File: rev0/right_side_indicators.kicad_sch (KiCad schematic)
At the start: 30 parts, among them IC1 ECP5-BGA256, U14 74AUP2G126, U2 74AUP2G126

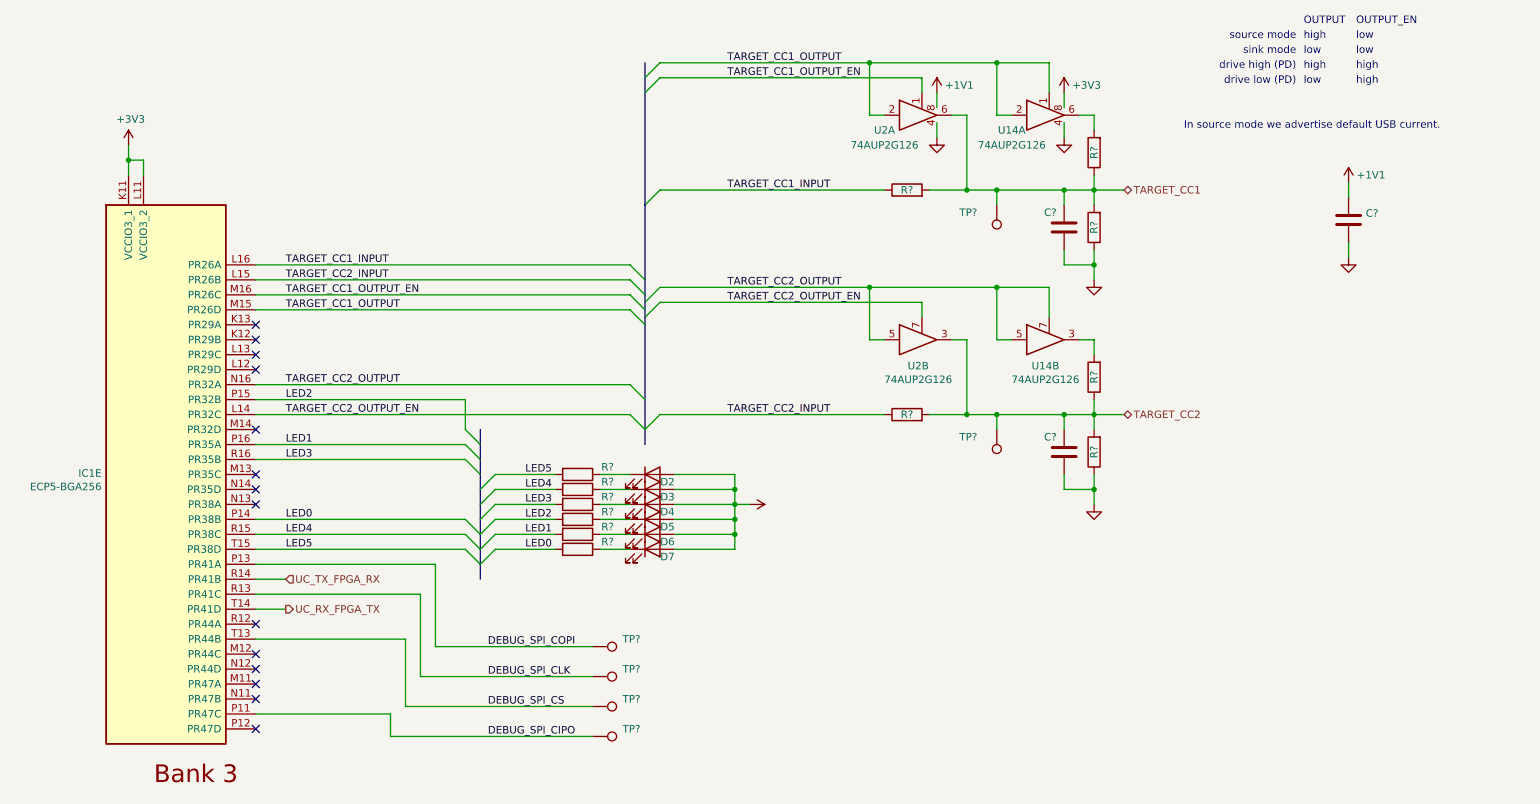
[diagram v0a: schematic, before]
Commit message: hardware: update 3D model paths for KiCad 6
see: https://gitlab.com/kicad/code/kicad/-/issues/10674
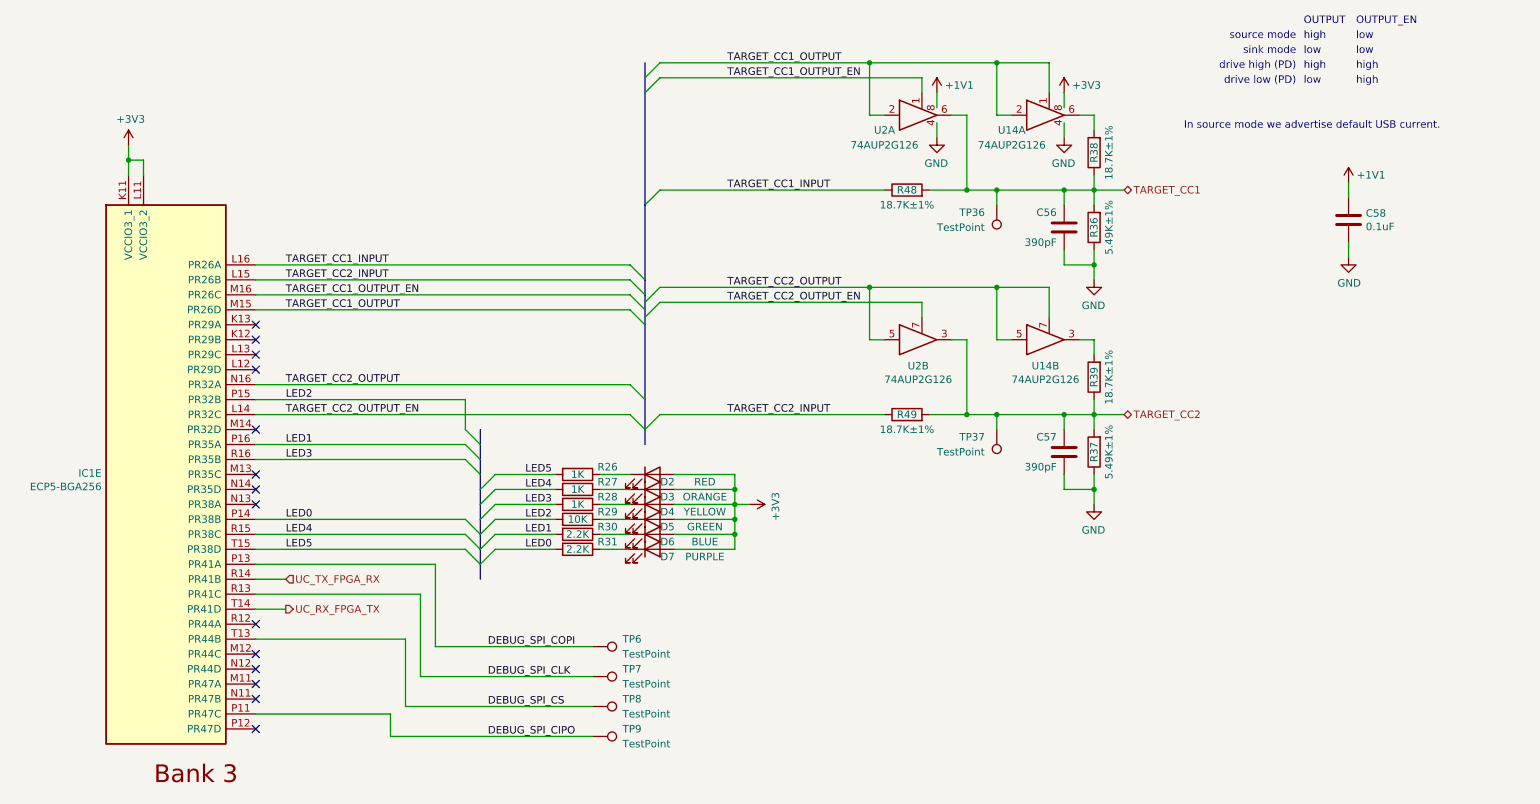
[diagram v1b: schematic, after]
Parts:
- C56, C57: renamed from C?; value (none) -> 390pF; footprint (none) -> Capacitor_SMD:C_0402_1005Metric
- C58: renamed from C?; value (none) -> 0.1uF; footprint (none) -> Capacitor_SMD:C_0402_1005Metric
- D2: value (none) -> RED; footprint (none) -> LED_SMD:LED_0603_1608Metric_Pad1.05x0.95mm_HandSolder
- D3: value (none) -> ORANGE; footprint (none) -> LED_SMD:LED_0603_1608Metric_Pad1.05x0.95mm_HandSolder
- D4: value (none) -> YELLOW; footprint (none) -> LED_SMD:LED_0603_1608Metric_Pad1.05x0.95mm_HandSolder
- D5: value (none) -> GREEN; footprint (none) -> LED_SMD:LED_0603_1608Metric_Pad1.05x0.95mm_HandSolder
- D6: value (none) -> BLUE; footprint (none) -> LED_SMD:LED_0603_1608Metric_Pad1.05x0.95mm_HandSolder
- D7: value (none) -> PURPLE; footprint (none) -> LED_SMD:LED_0603_1608Metric_Pad1.05x0.95mm_HandSolder
- R26, R27, R28: renamed from R?; value (none) -> 1K; footprint (none) -> Resistor_SMD:R_0402_1005Metric
- R29: renamed from R?; value (none) -> 10K; footprint (none) -> Resistor_SMD:R_0402_1005Metric
- R30, R31: renamed from R?; value (none) -> 2.2K; footprint (none) -> Resistor_SMD:R_0402_1005Metric
- R36, R37: renamed from R?; value (none) -> 5.49K±1%; footprint (none) -> Resistor_SMD:R_0402_1005Metric
- R38, R39, R48, R49: renamed from R?; value (none) -> 18.7K±1%; footprint (none) -> Resistor_SMD:R_0402_1005Metric
- TP36, TP37, TP6, TP7, TP8, TP9: renamed from TP?; value (none) -> TestPoint; footprint (none) -> TestPoint:TestPoint_Pad_D1.0mm

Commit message: hardware: update silkscreen, dates, title blocks
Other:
- company: Copyright 2019-2021 Great Scott Gadgets -> Copyright 2019-2023 Great Scott Gadgets
- title: LUNA: Right Side I/O -> LUNA USB Multitool
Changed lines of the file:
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@@
   (paper "A4")
   (title_block
-    (title "LUNA: Right Side I/O")
-    (date "2021-03-10")
-    (rev "r0")
-    (company "Copyright 2019-2021 Great Scott Gadgets")
-    (comment 1 "Katherine J. Temkin")
-    (comment 3 "Licensed under the CERN-OHL-P v2")
+    (title "LUNA USB Multitool")
+    (date "2023-01-11")
+    (rev "r0.5")
+    (company "Copyright 2019-2023 Great Scott Gadgets")
+    (comment 1 "Licensed under the CERN-OHL-P v2")
   )
   (junction (at 201.93 88.9) (diameter 0) (color 0 0 0 0)

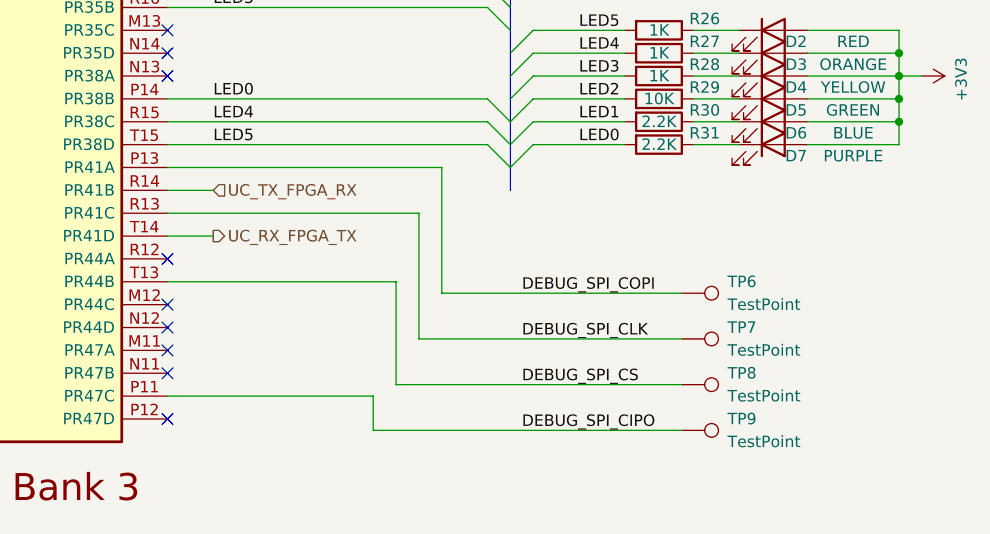
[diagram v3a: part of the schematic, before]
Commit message: hardware: remove debug SPI interface
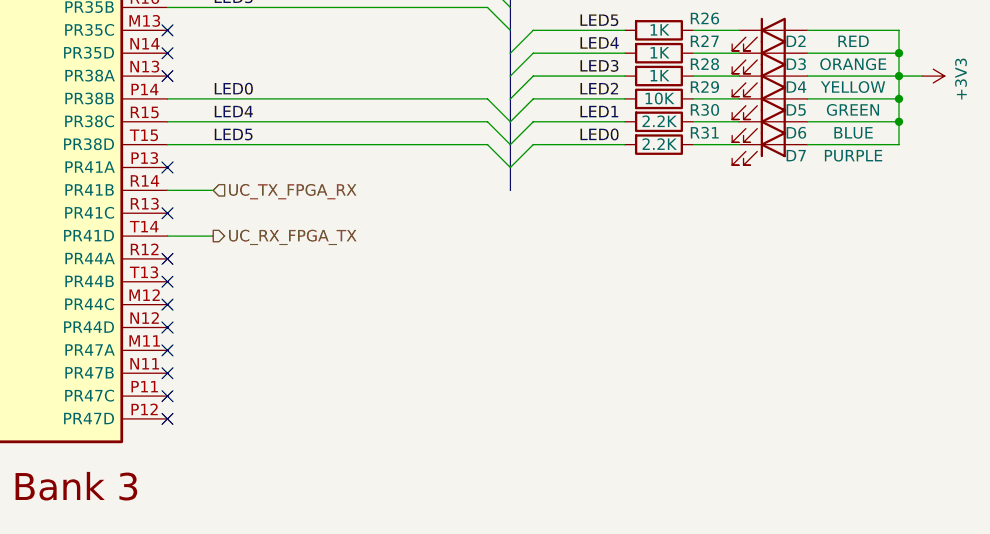
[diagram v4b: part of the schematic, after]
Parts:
- removed TP6, TP7, TP8, TP9: TestPoint, TestPoint:TestPoint_Pad_D1.0mm, symbol Connector:TestPoint
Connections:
- net DEBUG_SPI_CIPO: no longer names the net of IC1.P11 (PR47C)
- net DEBUG_SPI_CLK: no longer names the net of IC1.R13 (PR41C)
- net DEBUG_SPI_COPI: no longer names the net of IC1.P13 (PR41A)
- net DEBUG_SPI_CS: no longer names the net of IC1.T13 (PR44B)
- no-connect marks 14 -> 18
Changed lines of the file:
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@@
   )
   (no_connect (at 76.2 101.6))
+  (no_connect (at 76.2 119.38))
+  (no_connect (at 76.2 127))
   (no_connect (at 76.2 137.16))
   (no_connect (at 76.2 81.28))
   (no_connect (at 76.2 132.08))
+  (no_connect (at 76.2 139.7))
   (no_connect (at 76.2 76.2))
   (no_connect (at 76.2 134.62))
   (no_connect (at 76.2 104.14))
   (no_connect (at 76.2 129.54))
+  (no_connect (at 76.2 114.3))
   (no_connect (at 76.2 73.66))
   (no_connect (at 76.2 78.74))
@@
     (stroke (width 0) (type default) (color 0 0 0 0))
   )
-  (wire (pts (xy 99.06 143.51) (xy 99.06 139.7))
-    (stroke (width 0) (type default) (color 0 0 0 0))
-  )
   (wire (pts (xy 196.85 88.9) (xy 190.5 88.9))
     (stroke (width 0) (type default) (color 0 0 0 0))
@@
     (stroke (width 0) (type default) (color 0 0 0 0))
   )
-  (wire (pts (xy 76.2 127) (xy 101.6 127))
-    (stroke (width 0) (type default) (color 0 0 0 0))
-  )
   (wire (pts (xy 157.48 99.06) (xy 157.48 101.6))
     (stroke (width 0) (type default) (color 0 0 0 0))
@@
     (stroke (width 0) (type default) (color 0 0 0 0))
   )
-  (wire (pts (xy 104.14 133.35) (xy 133.35 133.35))
-    (stroke (width 0) (type default) (color 0 0 0 0))
-  )
   (bus (pts (xy 114.3 99.06) (xy 114.3 101.6))
     (stroke (width 0) (type default) (color 0 0 0 0))
@@
     (stroke (width 0) (type default) (color 0 0 0 0))
   )
-  (wire (pts (xy 106.68 128.27) (xy 106.68 114.3))
-    (stroke (width 0) (type default) (color 0 0 0 0))
-  )
   (wire (pts (xy 218.44 63.5) (xy 218.44 66.04))
     (stroke (width 0) (type default) (color 0 0 0 0))
@@
     (stroke (width 0) (type default) (color 0 0 0 0))
   )
-  (wire (pts (xy 104.14 119.38) (xy 104.14 133.35))
-    (stroke (width 0) (type default) (color 0 0 0 0))
-  )
-  (wire (pts (xy 101.6 138.43) (xy 101.6 127))
-    (stroke (width 0) (type default) (color 0 0 0 0))
-  )
   (bus (pts (xy 114.3 104.14) (xy 114.3 106.68))
     (stroke (width 0) (type default) (color 0 0 0 0))
@@
     (stroke (width 0) (type default) (color 0 0 0 0))
   )
-  (wire (pts (xy 76.2 114.3) (xy 106.68 114.3))
-    (stroke (width 0) (type default) (color 0 0 0 0))
-  )
   (wire (pts (xy 223.52 88.9) (xy 218.44 88.9))
     (stroke (width 0) (type default) (color 0 0 0 0))
@@
     (stroke (width 0) (type default) (color 0 0 0 0))
   )
-  (wire (pts (xy 76.2 139.7) (xy 99.06 139.7))
-    (stroke (width 0) (type default) (color 0 0 0 0))
-  )
   (wire (pts (xy 116.84 109.22) (xy 127 109.22))
     (stroke (width 0) (type default) (color 0 0 0 0))
@@
     (stroke (width 0) (type default) (color 0 0 0 0))
   )
-  (wire (pts (xy 133.35 143.51) (xy 99.06 143.51))
-    (stroke (width 0) (type default) (color 0 0 0 0))
-  )
   (bus (pts (xy 142.24 72.39) (xy 142.24 73.66))
     (stroke (width 0) (type default) (color 0 0 0 0))
@@
     (stroke (width 0) (type default) (color 0 0 0 0))
   )
-  (wire (pts (xy 106.68 128.27) (xy 133.35 128.27))
-    (stroke (width 0) (type default) (color 0 0 0 0))
-  )
   (wire (pts (xy 190.5 50.8) (xy 196.85 50.8))
     (stroke (width 0) (type default) (color 0 0 0 0))
@@
     (stroke (width 0) (type default) (color 0 0 0 0))
   )
-  (wire (pts (xy 101.6 138.43) (xy 133.35 138.43))
-    (stroke (width 0) (type default) (color 0 0 0 0))
-  )
   (wire (pts (xy 218.44 63.5) (xy 213.36 63.5))
     (stroke (width 0) (type default) (color 0 0 0 0))
@@
   )
   (wire (pts (xy 157.48 111.76) (xy 147.32 111.76))
-    (stroke (width 0) (type default) (color 0 0 0 0))
-  )
-  (wire (pts (xy 76.2 119.38) (xy 104.14 119.38))
     (stroke (width 0) (type default) (color 0 0 0 0))
   )
@@
     (effects (font (size 1.27 1.27)) (justify left bottom))
   )
-  (label "DEBUG_SPI_COPI" (at 115.57 128.27 0)
-    (effects (font (size 1.27 1.27)) (justify left bottom))
-  )
   (label "TARGET_CC1_OUTPUT" (at 81.28 71.12 0)
     (effects (font (size 1.27 1.27)) (justify left bottom))
@@
     (effects (font (size 1.27 1.27)) (justify left bottom))
   )
-  (label "DEBUG_SPI_CIPO" (at 115.57 143.51 0)
-    (effects (font (size 1.27 1.27)) (justify left bottom))
-  )
   (label "LED4" (at 121.92 101.6 0)
     (effects (font (size 1.27 1.27)) (justify left bottom))
@@
     (effects (font (size 1.27 1.27)) (justify left bottom))
   )
-  (label "DEBUG_SPI_CLK" (at 115.57 133.35 0)
-    (effects (font (size 1.27 1.27)) (justify left bottom))
-  )
   (label "LED3" (at 121.92 104.14 0)
     (effects (font (size 1.27 1.27)) (justify left bottom))
@@
   )
   (label "LED5" (at 81.28 111.76 0)
-    (effects (font (size 1.27 1.27)) (justify left bottom))
-  )
-  (label "DEBUG_SPI_CS" (at 115.57 138.43 0)
     (effects (font (size 1.27 1.27)) (justify left bottom))
   )
@@
     (pin "2")
   )
-  (symbol (lib_id "Connector:TestPoint") (at 133.35 138.43 270) (mirror x) (unit 1)
-    (in_bom yes) (on_board yes)
-    (property "Reference" "TP8" (id 0) (at 138.43 137.16 90)
-      (effects (font (size 1.27 1.27)) (justify left))
-    )
-    (property "Value" "TestPoint" (id 1) (at 138.43 139.7 90)
-      (effects (font (size 1.27 1.27)) (justify left))
-    )
-    (property "Footprint" "TestPoint:TestPoint_Pad_D1.0mm" (id 2) (at 133.35 133.35 0)
-      (effects (font (size 1.27 1.27)) hide)
-    )
-    (property "Datasheet" "~" (id 3) (at 133.35 133.35 0)
-      (effects (font (size 1.27 1.27)) hide)
-    )
-    (property "Note" "DNP" (id 4) (at 133.35 138.43 0)
-      (effects (font (size 1.27 1.27)) hide)
-    )
-    (pin "1")
-  )
-  (symbol (lib_id "Connector:TestPoint") (at 133.35 128.27 270) (mirror x) (unit 1)
-    (in_bom yes) (on_board yes)
-    (property "Reference" "TP6" (id 0) (at 138.43 127 90)
-      (effects (font (size 1.27 1.27)) (justify left))
-    )
-    (property "Value" "TestPoint" (id 1) (at 138.43 129.54 90)
-      (effects (font (size 1.27 1.27)) (justify left))
-    )
-    (property "Footprint" "TestPoint:TestPoint_Pad_D1.0mm" (id 2) (at 133.35 123.19 0)
-      (effects (font (size 1.27 1.27)) hide)
-    )
-    (property "Datasheet" "~" (id 3) (at 133.35 123.19 0)
-      (effects (font (size 1.27 1.27)) hide)
-    )
-    (property "Note" "DNP" (id 4) (at 133.35 128.27 0)
-      (effects (font (size 1.27 1.27)) hide)
-    )
-    (pin "1")
-  )
-  (symbol (lib_id "Connector:TestPoint") (at 133.35 133.35 270) (mirror x) (unit 1)
-    (in_bom yes) (on_board yes)
-    (property "Reference" "TP7" (id 0) (at 138.43 132.08 90)
-      (effects (font (size 1.27 1.27)) (justify left))
-    )
-    (property "Value" "TestPoint" (id 1) (at 138.43 134.62 90)
-      (effects (font (size 1.27 1.27)) (justify left))
-    )
-    (property "Footprint" "TestPoint:TestPoint_Pad_D1.0mm" (id 2) (at 133.35 128.27 0)
-      (effects (font (size 1.27 1.27)) hide)
-    )
-    (property "Datasheet" "~" (id 3) (at 133.35 128.27 0)
-      (effects (font (size 1.27 1.27)) hide)
-    )
-    (property "Note" "DNP" (id 4) (at 133.35 133.35 0)
-      (effects (font (size 1.27 1.27)) hide)
-    )
-    (pin "1")
-  )
-  (symbol (lib_id "Connector:TestPoint") (at 133.35 143.51 270) (mirror x) (unit 1)
-    (in_bom yes) (on_board yes)
-    (property "Reference" "TP9" (id 0) (at 138.43 142.24 90)
-      (effects (font (size 1.27 1.27)) (justify left))
-    )
-    (property "Value" "TestPoint" (id 1) (at 138.43 144.78 90)
-      (effects (font (size 1.27 1.27)) (justify left))
-    )
-    (property "Footprint" "TestPoint:TestPoint_Pad_D1.0mm" (id 2) (at 133.35 138.43 0)
-      (effects (font (size 1.27 1.27)) hide)
-    )
-    (property "Datasheet" "~" (id 3) (at 133.35 138.43 0)
-      (effects (font (size 1.27 1.27)) hide)
-    )
-    (property "Note" "DNP" (id 4) (at 133.35 143.51 0)
-      (effects (font (size 1.27 1.27)) hide)
-    )
-    (pin "1")
-  )
 )
